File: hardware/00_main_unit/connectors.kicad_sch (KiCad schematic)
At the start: 10 parts, among them J1 Conn_01x10, J10 USB B connector, J12 RJ45, J2 Conn_01x10, J3 Conn_01x10, J4 Conn_01x10, J7 Conn_01x10, J8 Conn_01x10, J9 RJ45

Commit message: Fixes before ordering PCB
Signed-off-by: Jarosław Karwik <jaroslaw.karwik@gmail.com>
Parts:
- J12, J9: TME 54602-910LF -> RJ45G
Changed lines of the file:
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@@
-    (stroke (width 0) (type solid) (color 0 0 0 0))
-  )
-  (wire (pts (xy 41.275 73.66) (xy 42.545 73.66))
     (stroke (width 0) (type solid) (color 0 0 0 0))
   )
@@
     (stroke (width 0) (type solid) (color 0 0 0 0))
   )
-  (wire (pts (xy 41.275 91.44) (xy 41.275 100.33))
-    (stroke (width 0) (type solid) (color 0 0 0 0))
-  )
   (wire (pts (xy 41.275 91.44) (xy 43.815 91.44))
     (stroke (width 0) (type solid) (color 0 0 0 0))
   )
+  (wire (pts (xy 41.275 100.33) (xy 41.275 91.44))
+    (stroke (width 0) (type solid) (color 0 0 0 0))
+  )
   (wire (pts (xy 41.275 100.33) (xy 41.275 105.41))
     (stroke (width 0) (type solid) (color 0 0 0 0))
@@
   )
   (wire (pts (xy 41.275 139.7) (xy 43.815 139.7))
+    (stroke (width 0) (type solid) (color 0 0 0 0))
+  )
+  (wire (pts (xy 42.545 73.66) (xy 41.275 73.66))
     (stroke (width 0) (type solid) (color 0 0 0 0))
   )
@@
       (effects (font (size 1.27 1.27)) hide)
     )
-    (property "TME" "54602-910LF" (id 4) (at 200.66 45.72 0)
+    (property "TME" "RJ45G" (id 4) (at 200.66 45.72 0)
       (effects (font (size 1.27 1.27)) hide)
     )
@@
       (effects (font (size 1.27 1.27)) hide)
     )
-    (property "TME" "54602-910LF" (id 4) (at 224.79 45.72 0)
-      (effects (font (size 1.27 1.27)) hide)
-    )
+    (property "TME" "RJ45G" (id 4) (at 224.79 45.72 0)
+      (effects (font (size 1.27 1.27)) hide)
+    )

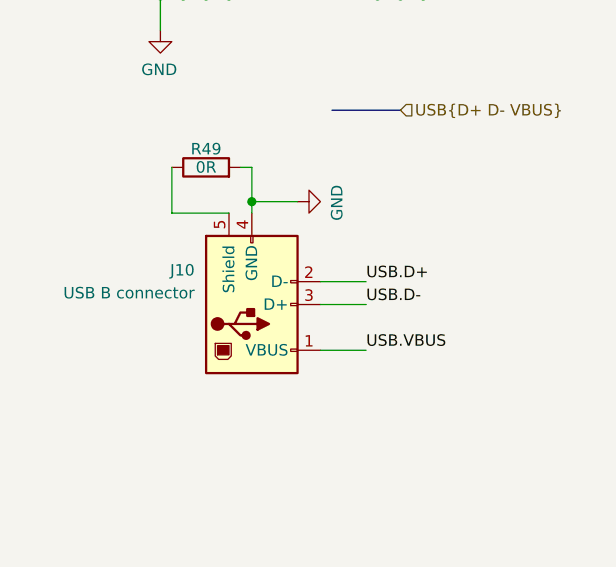
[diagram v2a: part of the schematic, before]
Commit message: Remote mode fixes
Signed-off-by: Jarosław Karwik <jaroslaw.karwik@gmail.com>
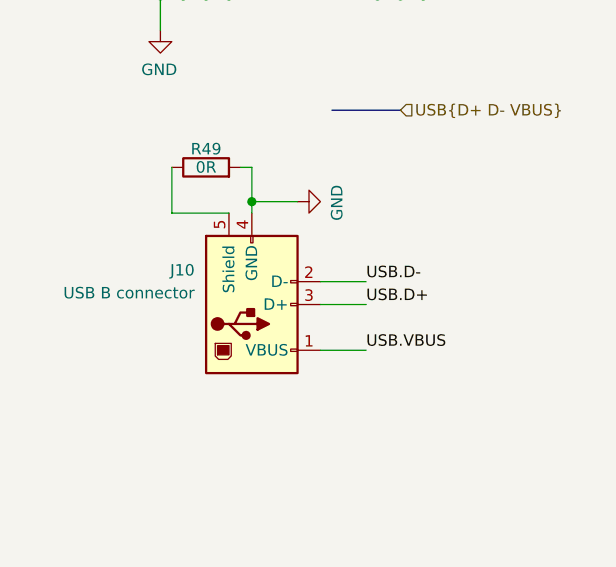
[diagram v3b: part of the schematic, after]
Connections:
- net USB.D+: now also J10.3 (D+); no longer J10.2 (D-)
- net USB.D-: now also J10.2 (D-); no longer J10.3 (D+)

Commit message: FW and SW updates for new revision
Signed-off-by: Jarosław Karwik <jaroslaw.karwik@gmail.com>
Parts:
- removed J12, J9: RJ45, Connector_RJ:RJ45_Amphenol_54602-x08_Horizontal, symbol Connector:RJ45
- added J14: Conn_01x10, moje:PhoenixContact_MC-G_10x3.50mm_Angled, symbol Uni_Printer-rescue:Conn_01x10-Connector_Generic
- added J16, J17, J18: RJ45_Shielded, Connector_RJ:RJ45_Ninigi_GE, symbol Connector:RJ45_Shielded
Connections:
- net +5V: now also J14.1 (Pin_1)
- net GND: now also J14.6 (Pin_6), J16.SH, J17.SH, J18.SH
- new net DIFF_IN.A1: J16.5
- new net DIFF_IN.A2: J16.2
- new net DIFF_IN.B1: J16.4
- new net DIFF_IN.B2: J16.1
- new net DIR3.A: J14.9 (Pin_9)
- new net DIR3.B: J14.10 (Pin_10)
- new net DIR4.A: J17.7
- new net DIR4.B: J17.8
- new net DIR5.A: J17.4
- new net DIR5.B: J17.5
- new net DIR6.A: J18.7
- new net DIR6.B: J18.8
- new net DIR7.A: J18.4
- new net DIR7.B: J18.5
- new net ENC3_IN.A1: J14.2 (Pin_2)
- new net ENC3_IN.A2: J14.4 (Pin_4)
- new net ENC3_IN.B1: J14.3 (Pin_3)
- new net ENC3_IN.B2: J14.5 (Pin_5)
- new net I2C_DIFF.SCL_RX: J16.7
- new net I2C_DIFF.SCL_TX: J16.8
- new net I2C_DIFF.SDA_TX: J16.6
- new net I2C_DIFF_SDA_RX: J16.3
- new net STEP3.A: J14.7 (Pin_7)
- new net STEP3.B: J14.8 (Pin_8)
- new net STEP4.A: J17.3
- new net STEP4.B: J17.6
- new net STEP5.A: J17.1
- new net STEP5.B: J17.2
- new net STEP6.A: J18.3
- new net STEP6.B: J18.6
- new net STEP7.A: J18.1
- new net STEP7.B: J18.2
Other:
- moved on the sheet: J10, R49
